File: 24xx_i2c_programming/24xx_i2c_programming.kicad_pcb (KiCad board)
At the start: 2 copper layers, 14 x 11.4 mm, 11 parts, among them J1 EXPANSION_BOTTOM, J2 A0, J3 A1, J4 A2, J5 WP, U1 24LC00

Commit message: Added helper text and a missing track to 24xx mod
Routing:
- net Net-(J5-Pad2): track 0.00 -> 2.83 mm, vias 0 -> 1
- net VCC: track 25.2 -> 26.0 mm
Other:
- board text added: "I2C"
- board text added: "this side up"
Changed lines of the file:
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@@
     (links 22)
     (no_connects 3)
-    (area 165.859 109.285 182.729 128.000762)
+    (area 166.929999 110.414999 181.050001 121.995001)
     (thickness 1.6)
-    (drawings 9)
-    (tracks 61)
+    (drawings 11)
+    (tracks 67)
     (zones 0)
     (modules 11)
@@
       (effects (font (size 1 1) (thickness 0.15)))
     )
-    (fp_text value WP (at -1.397 0.316 360) (layer F.SilkS)
+    (fp_text value WP (at 1.665 -0.495 540) (layer F.SilkS)
       (effects (font (size 0.7 0.7) (thickness 0.15)))
     )
@@
     )
   )
+  (gr_text "this\nside up" (at 178.6 111.9) (layer F.SilkS)
+    (effects (font (size 0.8 0.8) (thickness 0.2)))
+  )
+  (gr_text I2C (at 179.4 118.1 360) (layer F.SilkS)
+    (effects (font (size 1.2 1.2) (thickness 0.3)))
+  )
   (gr_text -> (at 168.148 112.014 320) (layer F.SilkS)
     (effects (font (size 0.8 0.8) (thickness 0.2)))
@@
   (gr_line (start 167.005 110.49) (end 180.975 110.49) (layer Edge.Cuts) (width 0.15))
   (gr_line (start 167.005 121.92) (end 167.005 110.49) (layer Edge.Cuts) (width 0.15))
+  (segment (start 179.705 114.935) (end 179.705 114.135) (width 0.25) (layer F.Cu) (net 1))
+  (segment (start 179.705 114.135) (end 179.755001 114.084999) (width 0.25) (layer F.Cu) (net 1))
   (segment (start 175.768 112.268) (end 175.448 112.268) (width 0.6) (layer F.Cu) (net 1))
   (segment (start 175.448 112.268) (end 174.94 111.76) (width 0.6) (layer F.Cu) (net 1))
@@
   (segment (start 170.434 116.205) (end 169.799 116.84) (width 0.25) (layer F.Cu) (net 7))
   (via (at 169.799 116.84) (size 0.6) (drill 0.4) (layers F.Cu B.Cu) (net 7))
+  (segment (start 178.3 114.935) (end 177.3145 114.935) (width 0.25) (layer B.Cu) (net 8))
+  (segment (start 177.165 114.935) (end 178.3 114.935) (width 0.25) (layer F.Cu) (net 8))
+  (segment (start 179.005 114.935) (end 178.3 114.935) (width 0.25) (layer F.Cu) (net 8))
+  (via (at 178.3 114.935) (size 0.6) (drill 0.4) (layers F.Cu B.Cu) (net 8))
 )

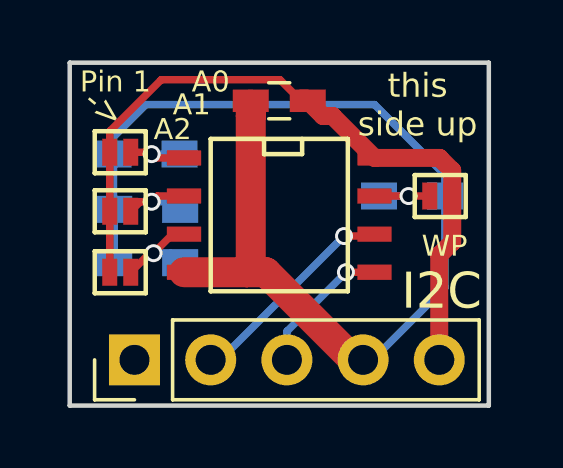
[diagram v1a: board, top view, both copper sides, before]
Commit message: Updating I2C pinout in 24xx EEPROM board
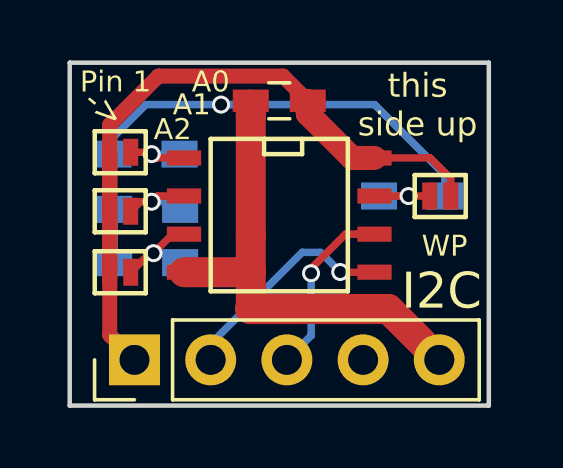
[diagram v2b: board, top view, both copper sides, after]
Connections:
- J1 pad 1: (no net) -> VCC
- J1 pad 2: SCL -> SDA
- J1 pad 3: SDA -> SCL
- J1 pad 4: GND -> (no net)
- J1 pad 5: VCC -> GND
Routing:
- net GND: track 37.2 -> 34.5 mm, vias 0 -> 1
- net SDA: track 5.01 -> 7.53 mm
- net VCC: track 26.0 -> 26.8 mm
- net SCL: track 7.33 -> 6.63 mm
